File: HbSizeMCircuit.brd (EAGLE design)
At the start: 47 x 55.9 mm, 24 parts

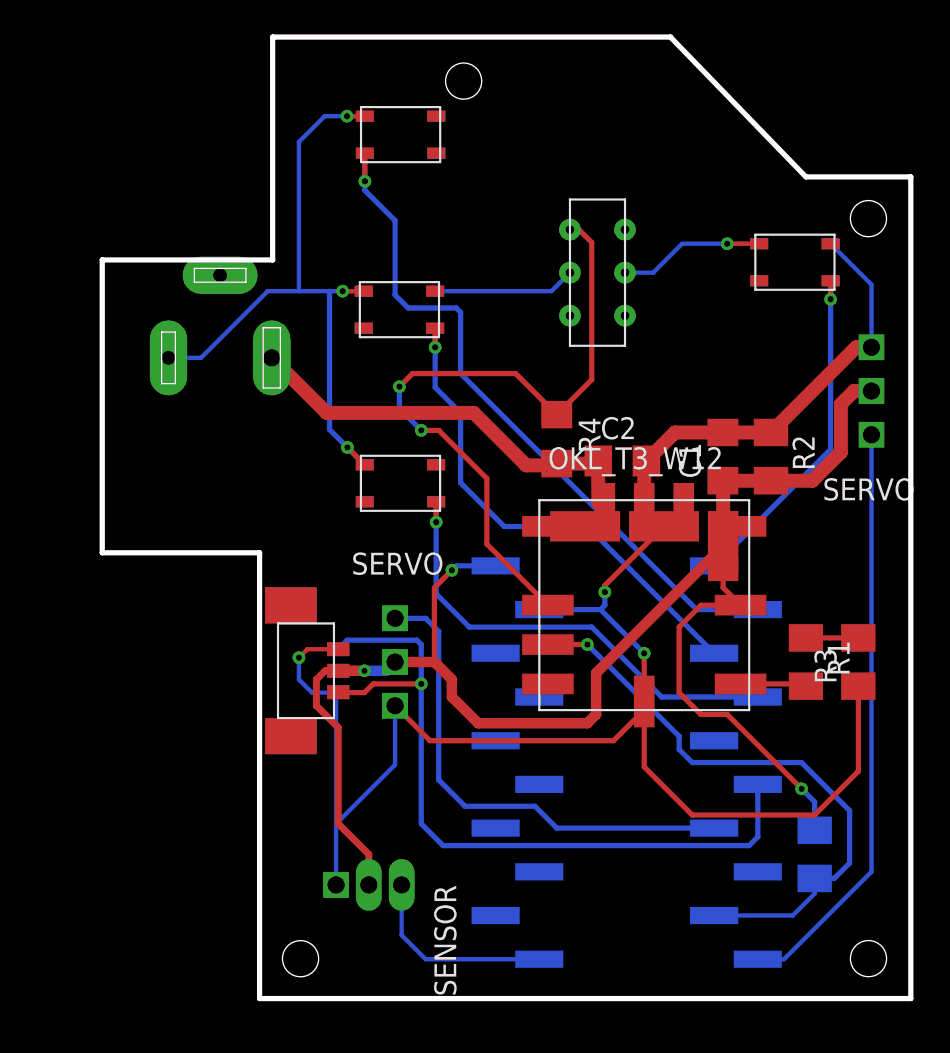
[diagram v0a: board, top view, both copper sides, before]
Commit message: DCジャックを変更
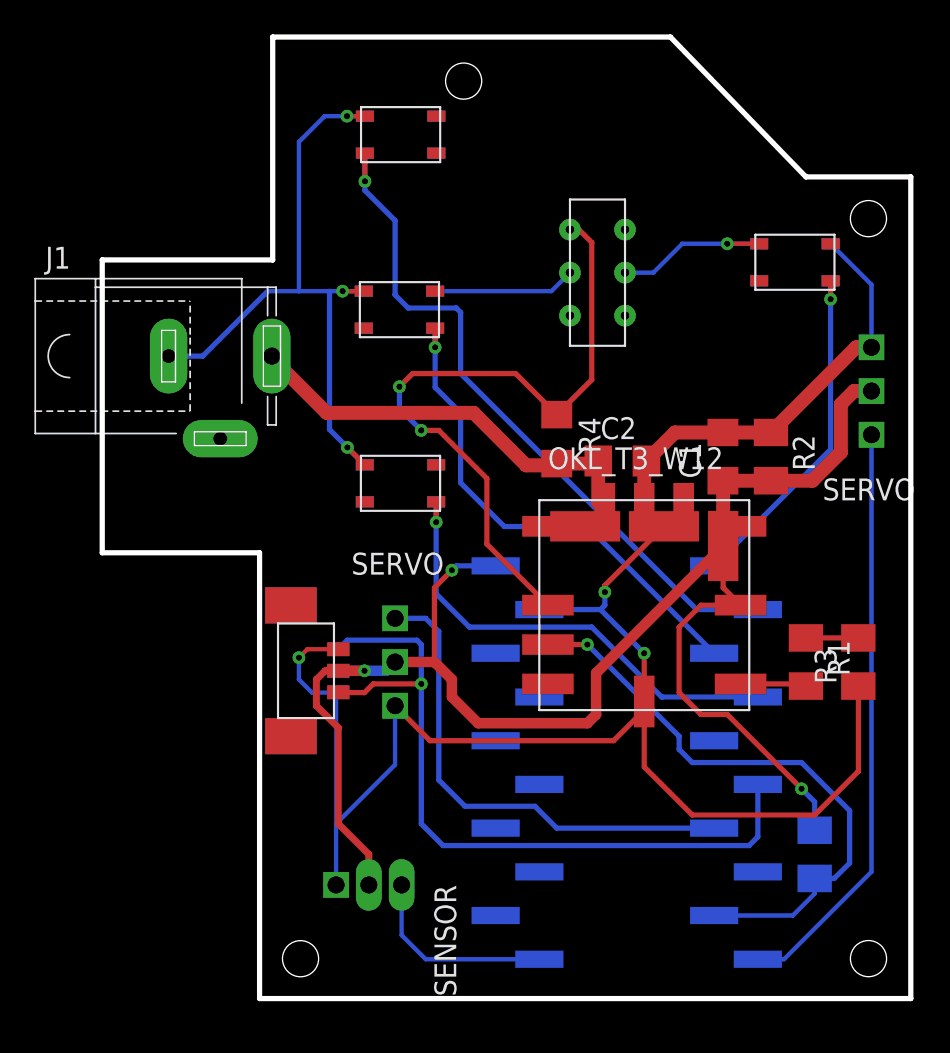
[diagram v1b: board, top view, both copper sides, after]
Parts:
- moved J1 0.10 mm to (7.11, 38.9), flipped to the top, turned to 0 degrees
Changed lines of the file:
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@@
 <layer number="44" name="Drills" color="7" fill="1" visible="no" active="yes"/>
 <layer number="45" name="Holes" color="7" fill="1" visible="yes" active="yes"/>
-<layer number="46" name="Milling" color="3" fill="1" visible="no" active="yes"/>
+<layer number="46" name="Milling" color="3" fill="1" visible="yes" active="yes"/>
 <layer number="47" name="Measures" color="7" fill="1" visible="no" active="yes"/>
 <layer number="48" name="Document" color="7" fill="1" visible="yes" active="yes"/>
@@
 <element name="C1" library="resistor" library_urn="urn:adsk.eagle:library:348" package="C1206" package3d_urn="urn:adsk.eagle:package:26140/1" value="10uF" x="36.322" y="33.02" rot="R90"/>
 <element name="C2" library="resistor" library_urn="urn:adsk.eagle:library:348" package="C1206" package3d_urn="urn:adsk.eagle:package:26140/1" value="22uF" x="30.48" y="32.766"/>
-<element name="J1" library="HbSizeM" package="SPC4078" value="" x="7.10438125" y="38.757859375" rot="MR180"/>
 <element name="R1" library="resistor" library_urn="urn:adsk.eagle:library:348" package="M1206" package3d_urn="urn:adsk.eagle:package:26088/1" value="1kΩ" x="41.148" y="21.082" rot="R270"/>
 <element name="R2" library="resistor" library_urn="urn:adsk.eagle:library:348" package="M1206" package3d_urn="urn:adsk.eagle:package:26088/1" value="1.2kΩ" x="39.116" y="33.02" rot="R270"/>
@@
 <element name="U$9" library="HbHandBoard_SizeS" package="53398-0371" value="53398-0371" x="13.97" y="20.574" rot="MR90"/>
 <element name="U$16" library="HbHandBoard_SizeS" package="53398-0371" value="53398-0371" x="13.97" y="20.574" rot="R270"/>
+<element name="J1" library="HbSizeM" package="SPC4078" value="" x="7.112" y="38.862"/>
 </elements>
 <signals>
 <signal name="V+">
-<contactref element="J1" pad="3"/>
 <contactref element="U$8" pad="PIN_2-1"/>
 <contactref element="U$8" pad="PIN_2-2"/>
@@
 <contactref element="C2" pad="1"/>
 <contactref element="R4" pad="2"/>
-<wire x1="10.10438125" y1="38.757859375" x2="13.302240625" y2="35.56" width="0.8128" layer="1"/>
 <wire x1="21.844" y1="35.56" x2="24.892" y2="32.512" width="0.8128" layer="1"/>
 <wire x1="24.892" y1="32.512" x2="26.568" y2="32.512" width="0.8128" layer="1"/>
 <wire x1="26.568" y1="32.512" x2="26.67" y2="32.614" width="0.8128" layer="1"/>
-<wire x1="13.302240625" y1="35.56" x2="21.844" y2="35.56" width="0.8128" layer="1"/>
+<wire x1="21.844" y1="35.56" x2="13.302240625" y2="35.56" width="0.8128" layer="1"/>
 <wire x1="26.67" y1="32.614" x2="28.928" y2="32.614" width="0.8128" layer="1"/>
 <wire x1="28.928" y1="32.614" x2="29.08" y2="32.766" width="0.8128" layer="1"/>
@@
 <wire x1="28.444" y1="28.968" x2="28.319" y2="28.968" width="0.3048" layer="1"/>
 <wire x1="28.319" y1="28.968" x2="26.154" y2="28.968" width="0.3048" layer="1"/>
+<contactref element="J1" pad="3"/>
+<wire x1="13.302240625" y1="35.56" x2="10.112" y2="38.750240625" width="0.8128" layer="1"/>
+<wire x1="10.112" y1="38.750240625" x2="10.112" y2="38.862" width="0.8128" layer="1"/>
 </signal>
 <signal name="GND">
@@
 <contactref element="U$10" pad="GND"/>
 <contactref element="U$16" pad="PIN_GND"/>
-<contactref element="J1" pad="1"/>
-<wire x1="4.10438125" y1="38.757859375" x2="5.991859375" y2="38.757859375" width="0.254" layer="16"/>
-<wire x1="9.86848125" y1="42.63448125" x2="11.684" y2="42.63448125" width="0.254" layer="16"/>
+<wire x1="11.684" y1="42.63448125" x2="9.86848125" y2="42.63448125" width="0.254" layer="16"/>
 <wire x1="11.684" y1="42.63448125" x2="13.462" y2="42.63448125" width="0.254" layer="16"/>
 <wire x1="13.462" y1="42.63448125" x2="14.224" y2="42.63448125" width="0.254" layer="16"/>
-<wire x1="5.991859375" y1="38.757859375" x2="9.86848125" y2="42.63448125" width="0.254" layer="16"/>
 <wire x1="14.478" y1="52.804640625" x2="13.180640625" y2="52.804640625" width="0.254" layer="16"/>
 <wire x1="11.684" y1="51.308" x2="11.684" y2="42.63448125" width="0.254" layer="16"/>
@@
 <wire x1="19.304" y1="16.51" x2="29.972" y2="16.51" width="0.3048" layer="1"/>
 <wire x1="29.972" y1="16.51" x2="31.754" y2="18.292" width="0.3048" layer="1"/>
-<wire x1="31.754" y1="18.292" x2="31.754" y2="18.542" width="0.3048" layer="1"/>
-<wire x1="31.754" y1="18.542" x2="31.754" y2="18.788" width="0.3048" layer="1"/>
+<wire x1="31.754" y1="18.292" x2="31.754" y2="18.788" width="0.3048" layer="1"/>
 <wire x1="25.654" y1="24.13" x2="29.21" y2="24.13" width="0.3048" layer="16"/>
 <wire x1="29.21" y1="24.13" x2="31.75" y2="21.59" width="0.3048" layer="16"/>
@@
 <vertex x="10.16" y="44.45"/>
 </polygon>
+<contactref element="J1" pad="1"/>
+<wire x1="9.86848125" y1="42.63448125" x2="6.096" y2="38.862" width="0.3048" layer="16"/>
+<wire x1="6.096" y1="38.862" x2="4.112" y2="38.862" width="0.3048" layer="16"/>
 </signal>
 <signal name="PIN_ON/OFF">
